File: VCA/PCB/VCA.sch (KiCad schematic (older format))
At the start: 64 parts

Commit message: cleaned up vca project
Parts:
- removed C? (x6): C, symbol C
- removed C? (x2): 100n, symbol C
- removed D? (x8): BAT54, Diodes_SMD:D_SOT-23_ANK, symbol D_ALT
- removed Q? (x2): BC846ASQ-T1, TO_SOT_Packages_SMD:SOT-363_SC-70-6_Handsoldering, symbol Q_DUAL_NPN_NPN_E1B1C2E2B2C1
- removed Q? (x2): BC846ASQ-T2, TO_SOT_Packages_SMD:SOT-363_SC-70-6_Handsoldering, symbol Q_DUAL_NPN_NPN_E1B1C2E2B2C1
- removed Q? (x2): Q_NPN_BCE, symbol Q_NPN_BCE
- removed R? (x16): 10k, Resistors_SMD:R_0603_HandSoldering, symbol R
- removed R? (x4): 100, Resistors_SMD:R_0603_HandSoldering, symbol R
- removed R? (x4): 100k, Resistors_SMD:R_0603_HandSoldering, symbol R
- removed R? (x2): 33k, Resistors_SMD:R_0603_HandSoldering, symbol R
- removed R? (x2): 15k, Resistors_SMD:R_0603_HandSoldering, symbol R
- removed R? (x2): 470, Resistors_SMD:R_0603_HandSoldering, symbol R
- removed R? (x2): 470k, Resistors_SMD:R_0603_HandSoldering, symbol R
- removed RV? (x2): 1k, Potentiometers:Potentiometer_Trimmer_Bourns_3299Y, symbol POT_TRIM
- removed RV? (x2): 100k, Potentiometers:Potentiometer_Trimmer_Bourns_3299Y, symbol POT_TRIM
- removed U? (x2): NE5532, Housings_SOIC:SO-8_5.3x6.2mm_Pitch1.27mm, symbol NE5532
- removed U? (x2): NE5532, symbol NE5532
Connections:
- net labels removed: +12V, -12V, GNDA, IN, OUT
- wire segments 176 -> 2
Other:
- note removed: "Input overvoltage protection"
- note removed: "Offset Correction"
- note removed: "balance correction"

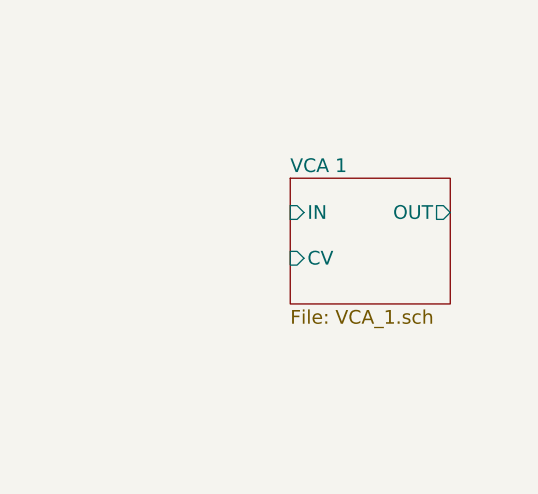
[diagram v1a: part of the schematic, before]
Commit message: scematic design of vca
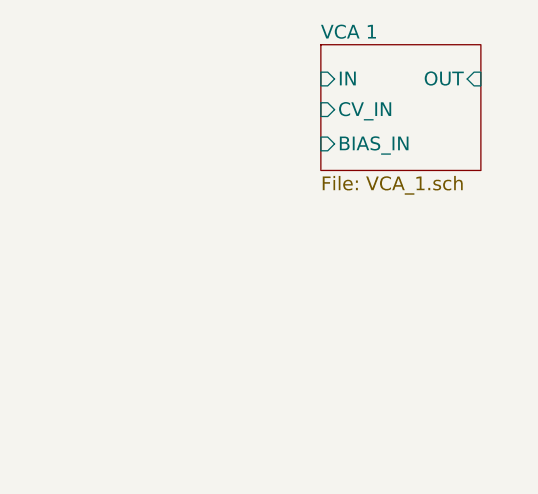
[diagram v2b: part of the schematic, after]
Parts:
- gave numbers to parts that had none: 2
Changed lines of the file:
@@
 $Descr A4 11693 8268
 encoding utf-8
-Sheet 1 3
+Sheet 1 2
 Title ""
 Date ""
@@
 $EndDescr
 $Comp
-L Audio-Jack-2 J?
+L Audio-Jack-2 J1
 U 1 1 61CB74DF
 P 1800 2750
-F 0 "J?" H 1775 2825 50  0000 C CNN
+F 0 "J1" H 1775 2825 50  0000 C CNN
 F 1 "Audio-Jack-2" H 1775 2575 50  0000 C CNN
 F 2 "" H 2050 2750 50  0001 C CNN
@@
 $EndComp
 $Comp
-L Earth #PWR?
+L Earth #PWR01
 U 1 1 61CB7B2E
 P 2100 3250
-F 0 "#PWR?" H 2100 3000 50  0001 C CNN
+F 0 "#PWR01" H 2100 3000 50  0001 C CNN
 F 1 "Earth" H 2100 3100 50  0001 C CNN
 F 2 "" H 2100 3250 50  0001 C CNN
@@
 	2100 2850 2000 2850
 $Comp
-L Audio-Jack-2 J?
+L Audio-Jack-2 J2
 U 1 1 61CDFC36
 P 1800 2750
-F 0 "J?" H 1775 2825 50  0000 C CNN
+F 0 "J2" H 1775 2825 50  0000 C CNN
 F 1 "Audio-Jack-2" H 1775 2575 50  0000 C CNN
 F 2 "" H 2050 2750 50  0001 C CNN
@@
 $EndComp
 $Comp
-L Earth #PWR?
+L Earth #PWR02
 U 1 1 61CDFC37
 P 2100 3250
-F 0 "#PWR?" H 2100 3000 50  0001 C CNN
+F 0 "#PWR02" H 2100 3000 50  0001 C CNN
 F 1 "Earth" H 2100 3100 50  0001 C CNN
 F 2 "" H 2100 3250 50  0001 C CNN
@@
 $EndComp
 $Sheet
-S 5400 2400 700  550
+S 5534 1816 700  550
 U 61CE060A
 F0 "VCA 1" 60
 F1 "VCA_1.sch" 60
-F2 "OUT" O R 6100 2550 60
-F3 "IN" I L 5400 2550 60
-F4 "CV" I L 5400 2750 60
+F2 "CV_IN" I L 5534 2100 60
+F3 "IN" I L 5534 1966 60
+F4 "OUT" I R 6234 1966 60
+F5 "BIAS_IN" I L 5534 2250 60
 $EndSheet
 $EndSCHEMATC
